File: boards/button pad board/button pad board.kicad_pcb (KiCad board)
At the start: 2 copper layers, 4 parts

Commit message: worked on the button board a bit
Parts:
- added D1: LED_RBGA, yarrboard:WURTH_LED_RGB_5050-6, F.Cu at (57.9, 105.0)
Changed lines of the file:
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@@
   (net 17 "R2")
   (net 18 "R3")
+  (net 19 "VCC")
   (footprint "yarrboard:BUTTONPAD-2X2" (layer "F.Cu")
     (at 145.72 96.52)
@@
     (descr "2X2 BUTTON PAD W/ RGB LEDS")
     (tags "2X2 BUTTON PAD W/ RGB LEDS")
+    (property "Mouser" "474-COM-07836 ")
     (property "Sheetfile" "button pad board.kicad_sch")
     (property "Sheetname" "")
@@
       (net 12 "+5V") (pintype "passive") (solder_mask_margin 0.1016))
   )
+  (footprint "yarrboard:WURTH_LED_RGB_5050-6" (layer "F.Cu")
+    (at 57.92978 104.98)
+    (descr "http://cdn.sparkfun.com/datasheets/Components/LED/5060BRG4.pdf")
+    (tags "RGB LED 5050-6")
+    (property "LCSC" "C784540")
+    (property "Mouser" " 710-150505M173300 ")
+    (property "Sheetfile" "button pad board.kicad_sch")
+    (property "Sheetname" "")
+    (property "ki_description" "RGB LED, 6 pin package")
+    (property "ki_keywords" "LED RGB diode")
+    (attr smd)
+    (fp_text reference "D1" (at 0 -3.5 180) (layer "F.SilkS")
+        (effects (font (size 1 1) (thickness 0.15)))
+    )
+    (fp_text value "LED_RBGA" (at 0 3.3) (layer "F.Fab")
+        (effects (font (size 1 1) (thickness 0.15)))
+    )
+    (fp_text user "${REFERENCE}" (at 0 0) (layer "F.Fab")
+        (effects (font (size 0.6 0.6) (thickness 0.06)))
+    )
+    (fp_line (start -3.6 -2.7) (end 2.5 -2.7)
+      (stroke (width 0.12) (type solid)) (layer "F.SilkS"))
+    (fp_line (start -3.6 -1.6) (end -3.6 -2.7)
+      (stroke (width 0.12) (type solid)) (layer "F.SilkS"))
+    (fp_line (start 2.5 2.7) (end -2.5 2.7)
+      (stroke (width 0.12) (type solid)) (layer "F.SilkS"))
+    (fp_line (start -3.65 -2.75) (end -3.65 2.75)
+      (stroke (width 0.05) (type solid)) (layer "F.CrtYd"))
+    (fp_line (start -3.65 2.75) (end 3.65 2.75)
+      (stroke (width 0.05) (type solid)) (layer "F.CrtYd"))
+    (fp_line (start 3.65 -2.75) (end -3.65 -2.75)
+      (stroke (width 0.05) (type solid)) (layer "F.CrtYd"))
+    (fp_line (start 3.65 2.75) (end 3.65 -2.75)
+      (stroke (width 0.05) (type solid)) (layer "F.CrtYd"))
+    (fp_line (start -2.5 -2.5) (end -2.5 2.5)
+      (stroke (width 0.1) (type solid)) (layer "F.Fab"))
+    (fp_line (start -2.5 -1.9) (end -1.9 -2.5)
+      (stroke (width 0.1) (type solid)) (layer "F.Fab"))
+    (fp_line (start -2.5 2.5) (end 2.5 2.5)
+      (stroke (width 0.1) (type solid)) (layer "F.Fab"))
+    (fp_line (start 2.5 -2.5) (end -2.5 -2.5)
+      (stroke (width 0.1) (type solid)) (layer "F.Fab"))
+    (fp_line (start 2.5 2.5) (end 2.5 -2.5)
+      (stroke (width 0.1) (type solid)) (layer "F.Fab"))
+    (fp_circle (center 0 0) (end 0 -1.9)
+      (stroke (width 0.1) (type solid)) (fill none) (layer "F.Fab"))
+    (pad "BA" smd rect (at 2.4 -1.7 90) (size 1.1 2) (layers "F.Cu" "F.Paste" "F.Mask")
+      (net 19 "VCC") (pintype "passive"))
+    (pad "BK" smd rect (at -2.4 -1.7 90) (size 1.1 2) (layers "F.Cu" "F.Paste" "F.Mask")
+      (net 1 "B0") (pintype "passive"))
+    (pad "GA" smd rect (at 2.4 1.7 90) (size 1.1 2) (layers "F.Cu" "F.Paste" "F.Mask")
+      (net 19 "VCC") (pintype "passive"))
+    (pad "GK" smd rect (at -2.4 1.7 90) (size 1.1 2) (layers "F.Cu" "F.Paste" "F.Mask")
+      (net 3 "G0") (pintype "passive"))
+    (pad "RA" smd rect (at 2.4 0 90) (size 1.1 2) (layers "F.Cu" "F.Paste" "F.Mask")
+      (net 19 "VCC") (pintype "passive"))
+    (pad "RK" smd rect (at -2.4 0 90) (size 1.1 2) (layers "F.Cu" "F.Paste" "F.Mask")
+      (net 5 "R0") (pintype "passive"))
+    (model "${KICAD6_3DMODEL_DIR}/LED_SMD.3dshapes/LED_RGB_5050-6.wrl"
+      (offset (xyz 0 0 0))
+      (scale (xyz 1 1 1))
+      (rotate (xyz 0 0 0))
+    )
+  )
   (footprint "yarrboard:BUTTONPAD-2X2" (layer "F.Cu")

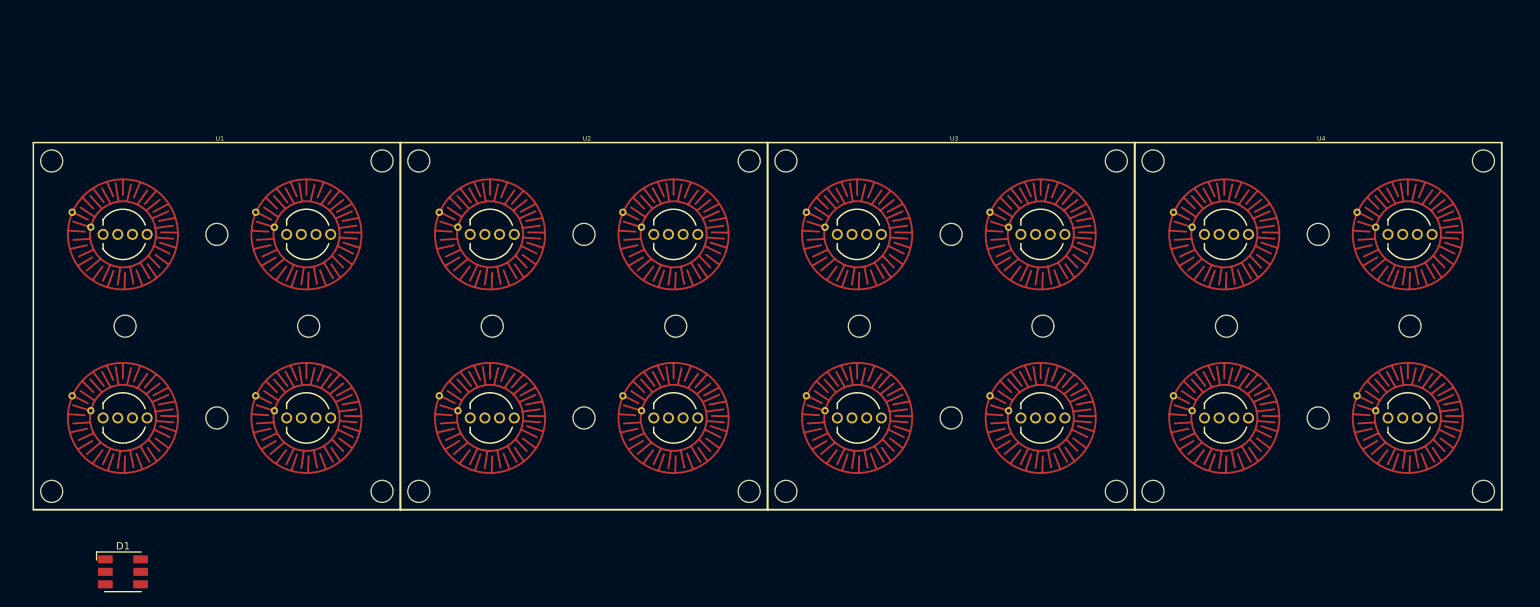
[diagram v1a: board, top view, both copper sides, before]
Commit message: changed to 5050 led for interface board
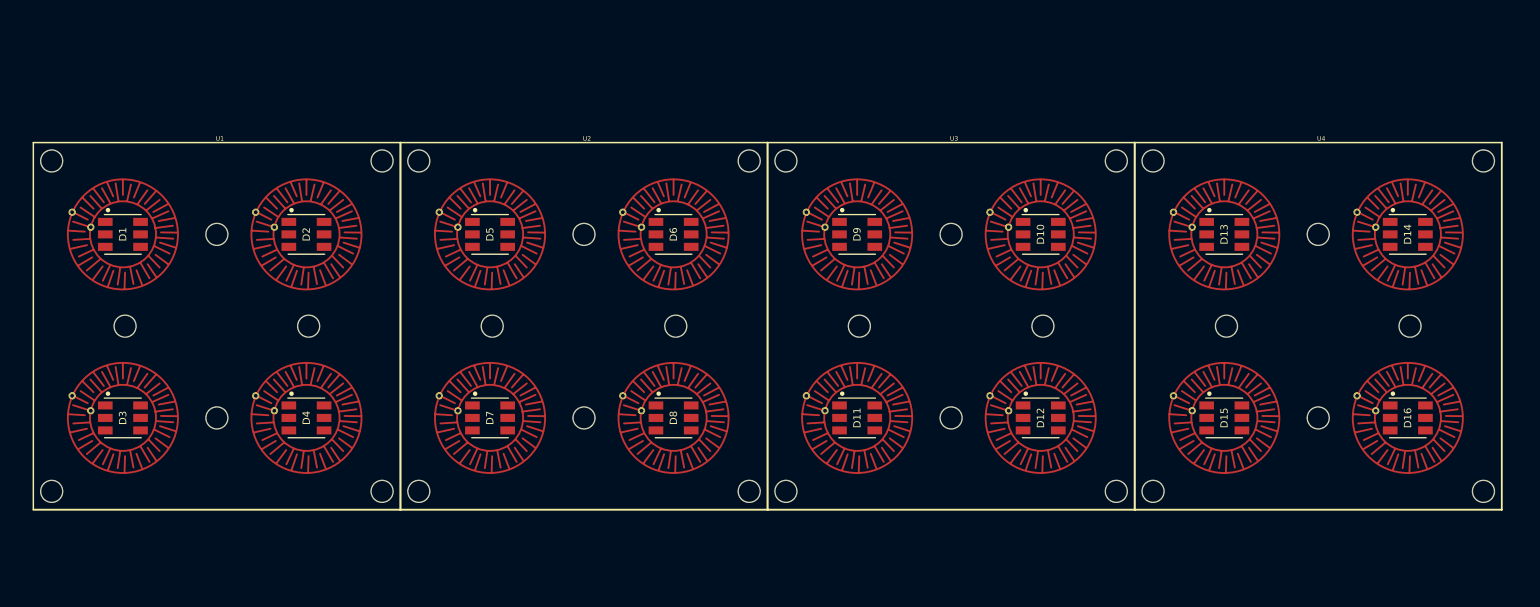
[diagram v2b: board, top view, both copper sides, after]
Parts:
- added D10: LED_RBGA, yarrboard:WURTH_LED_RGB_5050-6, F.Cu at (182.9, 59.0)
- added D11: LED_RBGA, yarrboard:WURTH_LED_RGB_5050-6, F.Cu at (157.9, 84.0)
- added D12: LED_RBGA, yarrboard:WURTH_LED_RGB_5050-6, F.Cu at (182.9, 84.0)
- added D13: LED_RBGA, yarrboard:WURTH_LED_RGB_5050-6, F.Cu at (207.9, 59.0)
- added D14: LED_RBGA, yarrboard:WURTH_LED_RGB_5050-6, F.Cu at (232.9, 59.0)
- added D15: LED_RBGA, yarrboard:WURTH_LED_RGB_5050-6, F.Cu at (207.9, 84.0)
- added D16: LED_RBGA, yarrboard:WURTH_LED_RGB_5050-6, F.Cu at (232.9, 84.0)
- added D2: LED_RBGA, yarrboard:WURTH_LED_RGB_5050-6, F.Cu at (82.9, 59.0)
- added D3: LED_RBGA, yarrboard:WURTH_LED_RGB_5050-6, F.Cu at (57.9, 84.0)
- added D4: LED_RBGA, yarrboard:WURTH_LED_RGB_5050-6, F.Cu at (82.9, 84.0)
- added D5: LED_RBGA, yarrboard:WURTH_LED_RGB_5050-6, F.Cu at (107.9, 59.0)
- added D6: LED_RBGA, yarrboard:WURTH_LED_RGB_5050-6, F.Cu at (132.9, 59.0)
- added D7: LED_RBGA, yarrboard:WURTH_LED_RGB_5050-6, F.Cu at (107.9, 84.0)
- added D8: LED_RBGA, yarrboard:WURTH_LED_RGB_5050-6, F.Cu at (132.9, 84.0)
- added D9: LED_RBGA, yarrboard:WURTH_LED_RGB_5050-6, F.Cu at (157.9, 59.0)
- moved D1 46.0 mm to (57.9, 59.0)
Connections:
- D1 pad BK: B0 -> /4x4 Button/B0
- D1 pad GK: G0 -> /4x4 Button/G0
- D1 pad RK: R0 -> /4x4 Button/R0
- U1 pad SWA1: IN0 -> /4x4 Button/SW0
- U1 pad SWA2: IN1 -> /4x4 Button/SW1
- U1 pad SWA3: IN2 -> /4x4 Button/SW2
- U1 pad SWA4: IN3 -> /4x4 Button/SW3
- U2 pad SWA1: IN0 -> /4x4 Button1/SW0
- U2 pad SWA2: IN1 -> /4x4 Button1/SW1
- U2 pad SWA3: IN2 -> /4x4 Button1/SW2
- U2 pad SWA4: IN3 -> /4x4 Button1/SW3
- U3 pad SWA1: IN0 -> /4x4 Button2/SW0
- U3 pad SWA2: IN1 -> /4x4 Button2/SW1
- U3 pad SWA3: IN2 -> /4x4 Button2/SW2
- U3 pad SWA4: IN3 -> /4x4 Button2/SW3
- U4 pad SWA1: IN0 -> /4x4 Button3/SW0
- U4 pad SWA2: IN1 -> /4x4 Button3/SW1
- U4 pad SWA3: IN2 -> /4x4 Button3/SW2
- U4 pad SWA4: IN3 -> /4x4 Button3/SW3

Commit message: good progress on teh button board
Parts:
- added J1: RGB, Connector_IDC:IDC-Header_2x25_P2.54mm_Horizontal, B.Cu at (115.6, 92.7)
- added J2: INPUTS, Connector_IDC:IDC-Header_2x10_P2.54mm_Horizontal, B.Cu at (209.6, 92.7)
- moved D11 5.08 mm to (157.9, 78.9)
- moved D12 5.08 mm to (182.9, 78.9)
- moved D15 5.08 mm to (207.9, 78.9)
- moved D16 5.08 mm to (232.9, 78.9)
- moved D3 5.08 mm to (57.9, 78.9)
- moved D4 5.08 mm to (82.9, 78.9)
- moved D7 5.08 mm to (107.9, 78.9)
- moved D8 5.08 mm to (132.9, 78.9)
- moved D1 5.08 mm to (57.9, 53.9)
- moved D10 5.08 mm to (182.9, 53.9)
- moved D13 5.08 mm to (207.9, 53.9)
- moved D14 5.08 mm to (232.9, 53.9)
- moved D2 5.08 mm to (82.9, 53.9)
- moved D5 5.08 mm to (107.9, 53.9)
- moved D6 5.08 mm to (132.9, 53.9)
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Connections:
- net VCC renamed +5V
- D1 pad BK: /4x4 Button/B0 -> B0
- D1 pad GK: /4x4 Button/G0 -> G0
- D1 pad RK: /4x4 Button/R0 -> R0
- D10 pad BK: /4x4 Button2/B1 -> B9
- D10 pad GK: /4x4 Button2/G1 -> G9
- D10 pad RK: /4x4 Button2/R1 -> R9
- D11 pad BK: /4x4 Button2/B2 -> B10
- D11 pad GK: /4x4 Button2/G2 -> G10
- D11 pad RK: /4x4 Button2/R2 -> R10
- D12 pad BK: /4x4 Button2/B3 -> B11
- D12 pad GK: /4x4 Button2/G3 -> G11
- D12 pad RK: /4x4 Button2/R3 -> R11
- D13 pad BK: /4x4 Button3/B0 -> B12
- D13 pad GK: /4x4 Button3/G0 -> G12
- D13 pad RK: /4x4 Button3/R0 -> R12
- D14 pad BK: /4x4 Button3/B1 -> B13
- D14 pad GK: /4x4 Button3/G1 -> G13
- D14 pad RK: /4x4 Button3/R1 -> R13
- D15 pad BK: /4x4 Button3/B2 -> B14
- D15 pad GK: /4x4 Button3/G2 -> G14
- D15 pad RK: /4x4 Button3/R2 -> R14
- D16 pad BK: /4x4 Button3/B3 -> B15
- D16 pad GK: /4x4 Button3/G3 -> G15
- D16 pad RK: /4x4 Button3/R3 -> R15
- D2 pad BK: /4x4 Button/B1 -> B1
- D2 pad GK: /4x4 Button/G1 -> G1
- D2 pad RK: /4x4 Button/R1 -> R1
- D3 pad BK: /4x4 Button/B2 -> B2
- D3 pad GK: /4x4 Button/G2 -> G2
- D3 pad RK: /4x4 Button/R2 -> R2
- D4 pad BK: /4x4 Button/B3 -> B3
- D4 pad GK: /4x4 Button/G3 -> G3
- D4 pad RK: /4x4 Button/R3 -> R3
- D5 pad BK: /4x4 Button1/B0 -> B4
- D5 pad GK: /4x4 Button1/G0 -> G4
- D5 pad RK: /4x4 Button1/R0 -> R4
- D6 pad BK: /4x4 Button1/B1 -> B5
- D6 pad GK: /4x4 Button1/G1 -> G5
- D6 pad RK: /4x4 Button1/R1 -> R5
- D7 pad BK: /4x4 Button1/B2 -> B6
- D7 pad GK: /4x4 Button1/G2 -> G6
- D7 pad RK: /4x4 Button1/R2 -> R6
- D8 pad BK: /4x4 Button1/B3 -> B7
- D8 pad GK: /4x4 Button1/G3 -> G7
- D8 pad RK: /4x4 Button1/R3 -> R7
- D9 pad BK: /4x4 Button2/B0 -> B8
- D9 pad GK: /4x4 Button2/G0 -> G8
- D9 pad RK: /4x4 Button2/R0 -> R8
- U1 pad SWA1: /4x4 Button/SW0 -> SW0
- U1 pad SWA2: /4x4 Button/SW1 -> SW1
- U1 pad SWA3: /4x4 Button/SW2 -> SW2
- U1 pad SWA4: /4x4 Button/SW3 -> SW3
- U2 pad SWA1: /4x4 Button1/SW0 -> SW4
- U2 pad SWA2: /4x4 Button1/SW1 -> SW5
- U2 pad SWA3: /4x4 Button1/SW2 -> SW6
- U2 pad SWA4: /4x4 Button1/SW3 -> SW7
- U3 pad SWA1: /4x4 Button2/SW0 -> SW8
- U3 pad SWA2: /4x4 Button2/SW1 -> SW9
- U3 pad SWA3: /4x4 Button2/SW2 -> SW10
- U3 pad SWA4: /4x4 Button2/SW3 -> SW11
- U4 pad SWA1: /4x4 Button3/SW0 -> SW12
- U4 pad SWA2: /4x4 Button3/SW1 -> SW13
- U4 pad SWA3: /4x4 Button3/SW2 -> SW14
- U4 pad SWA4: /4x4 Button3/SW3 -> SW15
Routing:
- net +5V: track 0.00 -> 51.8 mm, vias 0 -> 16
- net G3: track 0.00 -> 1.94 mm, vias 0 -> 1
- net G7: track 0.00 -> 1.94 mm, vias 0 -> 1
- net G15: track 0.00 -> 1.94 mm, vias 0 -> 1
- net G11: track 0.00 -> 1.94 mm, vias 0 -> 1
- net B3: track 0.00 -> 1.89 mm, vias 0 -> 1
- net B7: track 0.00 -> 1.89 mm, vias 0 -> 1
- net B15: track 0.00 -> 1.89 mm, vias 0 -> 1
- net B11: track 0.00 -> 1.89 mm, vias 0 -> 1
- net G8: track 0.00 -> 1.73 mm, vias 0 -> 1
- net G4: track 0.00 -> 1.73 mm, vias 0 -> 1
- net G12: track 0.00 -> 1.73 mm, vias 0 -> 1
- net G0: track 0.00 -> 1.73 mm, vias 0 -> 1
- net G1: track 0.00 -> 1.73 mm, vias 0 -> 1
- net G9: track 0.00 -> 1.73 mm, vias 0 -> 1
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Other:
- board outline added: 200 x 55.2 mm

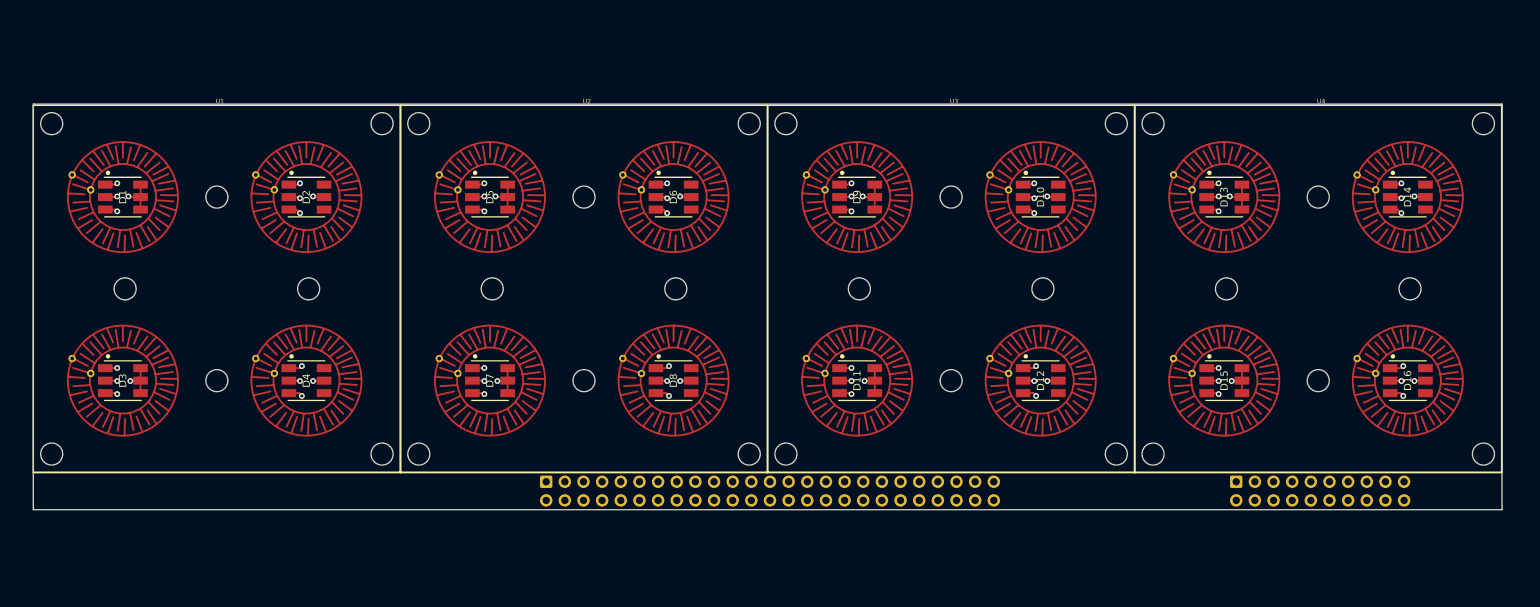
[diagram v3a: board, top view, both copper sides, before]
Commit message: working on routing the board rgb input board
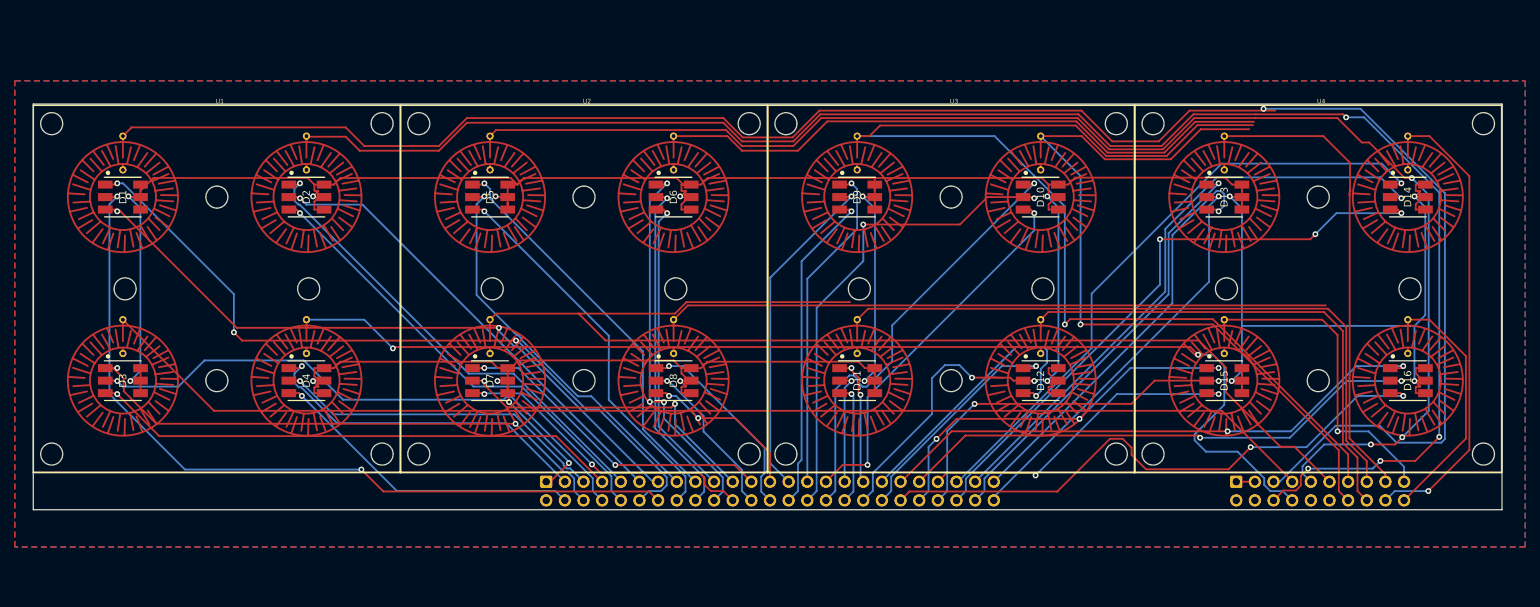
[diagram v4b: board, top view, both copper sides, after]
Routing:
- net +5V: track 51.8 -> 521.7 mm, vias 16 -> 18
- net SW0: track 0.00 -> 257.1 mm, vias 0 -> 1
- net SW1: track 0.00 -> 227.4 mm, vias 0 -> 4
- net SW4: track 0.00 -> 190.8 mm, vias 0 -> 3
- net SW2: track 0.00 -> 168.4 mm
- net SW6: track 0.00 -> 163.8 mm
- net SW3: track 0.00 -> 156.8 mm, vias 0 -> 2
- net SW8: track 0.00 -> 156.5 mm, vias 0 -> 1
- net SW9: track 0.00 -> 108.9 mm, vias 0 -> 1
- net R0: track 1.67 -> 109.7 mm, vias 1 -> 2
- net B0: track 1.70 -> 101.8 mm, vias 1 -> 3
- net SW10: track 0.00 -> 90.5 mm
- net SW7: track 0.00 -> 89.6 mm
- net G0: track 1.73 -> 90.9 mm, vias 1 -> 2
- net SW5: track 0.00 -> 85.0 mm
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- added copper zone on B.Cu, net GND
- added copper zone on F.Cu, net GND

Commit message: button board updated, routed, and ready to rock.
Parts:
- removed D10, D11, D12, D13, D14, D15, D16, D9: LED_RBGA, yarrboard:WURTH_LED_RGB_5050-6
- removed J2: INPUTS, Connector_IDC:IDC-Header_2x10_P2.54mm_Horizontal
- removed U3, U4: ~, yarrboard:BUTTONPAD-2X2
- added H1: MountingHole, MountingHole:MountingHole_3.2mm_M3_DIN965_Pad, F.Cu at (143.7, 93.5)
- added H2: MountingHole, MountingHole:MountingHole_3.2mm_M3_DIN965_Pad, F.Cu at (48.7, 93.5)
- added H3: MountingHole, MountingHole:MountingHole_3.2mm_M3_DIN965_Pad, F.Cu at (143.7, 37.5)
- added H4: MountingHole, MountingHole:MountingHole_3.2mm_M3_DIN965_Pad, F.Cu at (48.7, 37.5)
- added J3: INPUTS, Connector_FFC-FPC:TE_1-84952-0_1x10-1MP_P1.0mm_Horizontal, F.Cu at (150.7, 85.5)
- added REF**: Logo Small, yarrboard:Logo Small, F.Cu at (95.7, 65.5)
- J1: footprint Connector_IDC:IDC-Header_2x25_P2.54mm_Horizontal -> Connector_FFC-FPC:TE_3-84952-0_1x30-1MP_P1.0mm_Horizontal; moved to F.Cu
- moved J1 51.5 mm to (150.7, 55.0), turned to 90 degrees
- moved D1 1.00 mm to (57.9, 52.9)
- moved D2 1.00 mm to (82.9, 52.9)
- moved D3 1.00 mm to (57.9, 77.9)
- moved D4 1.00 mm to (82.9, 77.9)
- moved D5 1.00 mm to (107.9, 52.9)
- moved D6 1.00 mm to (132.9, 52.9)
- moved D7 1.00 mm to (107.9, 77.9)
- moved D8 1.00 mm to (132.9, 77.9)
- moved U1 1.00 mm to (45.7, 90.4)
- moved U2 1.00 mm to (95.7, 90.4)
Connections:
- J1 pad 10: G1 -> R1
- J1 pad 11: R1 -> G1
- J1 pad 12: B0 -> B1
- J1 pad 13: G0 -> R2
- J1 pad 14: R0 -> G2
- J1 pad 15: R4 -> B2
- J1 pad 16: G4 -> R3
- J1 pad 17: B4 -> G3
- J1 pad 18: R5 -> B3
- J1 pad 19: G5 -> R4
- J1 pad 2: GND -> +5V
- J1 pad 20: B5 -> G4
- J1 pad 21: R6 -> B4
- J1 pad 22: G6 -> R5
- J1 pad 23: B6 -> G5
- J1 pad 24: R7 -> B5
- J1 pad 25: G7 -> R6
- J1 pad 26: B7 -> G6
- J1 pad 27: R8 -> B6
- J1 pad 28: G8 -> R7
- J1 pad 29: B8 -> G7
- J1 pad 3: B3 -> +5V
- J1 pad 30: R9 -> B7
- J1 pad 4: G3 -> GND
- J1 pad 5: R3 -> GND
- J1 pad 6: B2 -> GND
- J1 pad 7: G2 -> R0
- J1 pad 8: R2 -> G0
- J1 pad 9: B1 -> B0
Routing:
- net +5V: track 521.7 -> 320.5 mm, vias 18 -> 12
- net SW8: track 156.5 -> 0.00 mm, vias 1 -> 0
- net SW0: track 257.1 -> 143.3 mm, vias 1 -> 0
- net SW9: track 108.9 -> 0.00 mm, vias 1 -> 0
- net SW1: track 227.4 -> 122.1 mm, vias 4 -> 1
- net SW4: track 190.8 -> 91.3 mm, vias 3 -> 1
- net SW6: track 163.8 -> 65.5 mm, vias 0 -> 1
- net SW10: track 90.5 -> 0.00 mm
- net B13: track 85.6 -> 0.00 mm, vias 1 -> 0
- net G13: track 83.1 -> 0.00 mm, vias 3 -> 0
- net R13: track 83.0 -> 0.00 mm, vias 1 -> 0
- net G15: track 80.3 -> 0.00 mm, vias 2 -> 0
- net B15: track 76.9 -> 0.00 mm, vias 2 -> 0
- net R15: track 73.2 -> 0.00 mm, vias 2 -> 0
- net SW11: track 67.1 -> 0.00 mm
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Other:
- board size 200 x 55.2 mm -> 114 x 62 mm
- board text added: "RGB LEDS"
- board text added: "SWITCHES"
- board text added: "Yarrboard RGB Button Pad Rev A"
- board text added: "github.com/hoeken/yarrboard"
